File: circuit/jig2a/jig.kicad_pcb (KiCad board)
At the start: 2 copper layers, 70 x 38 mm, 34 parts, among them J1 HOST_DEBUG, J10 S13, J11 S13, J12 S13, J13 S13, J14 S13, J15 S13, J16 S13, J17 S13, J18 S13, J19 S13, J2 HOST_UART, J20 S13, J21 S13, J22 S13, J23 S13, J3 HOST_POWER, J4 HOST_LEDS, J5 S13, J6 S13, J7 S13, J8 S13, J9 S13

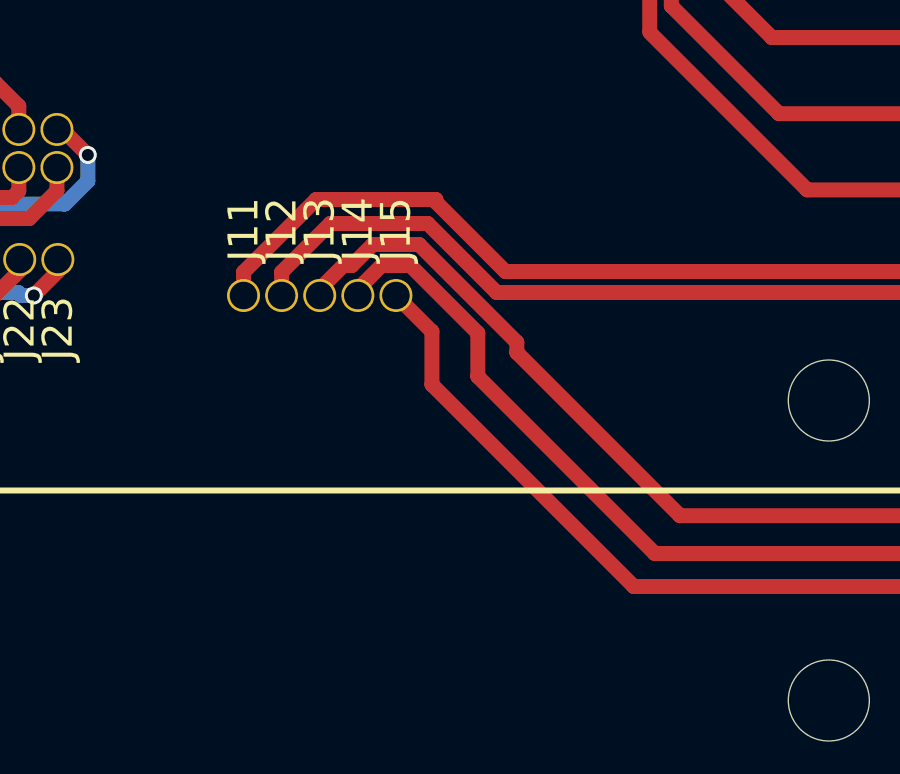
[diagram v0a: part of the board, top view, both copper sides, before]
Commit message: jig: Correct positioning of power debug pins
Signed-off-by: Gavan Fantom <gavan.fantom@unipart.io>
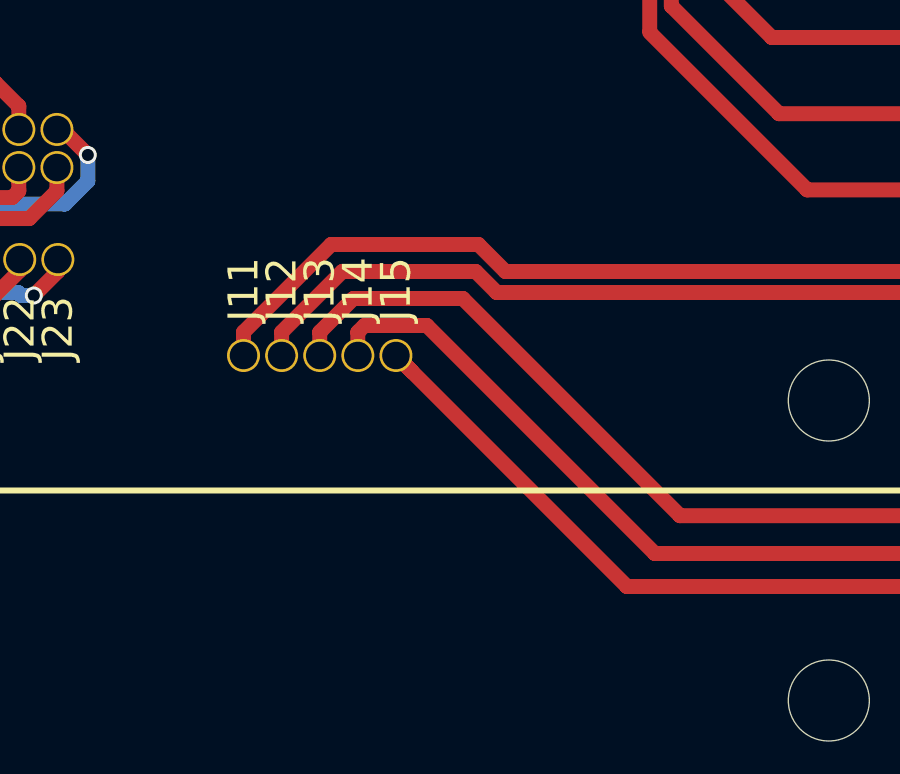
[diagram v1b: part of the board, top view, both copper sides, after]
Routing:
- net Net-(J14-Pad1): track 34.6 -> 33.2 mm
- net Net-(J15-Pad1): track 33.7 -> 32.6 mm
- net Net-(J13-Pad1): track 34.7 -> 34.2 mm
